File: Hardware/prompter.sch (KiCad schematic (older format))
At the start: 76 parts, among them J1 USB_B_Micro, J2 SWD, J3 L1, J4 L3, J5 PWR, J6 L2, J7 L4, J8 UART, Q1 AO3401A, SW1 PGM/RUN, SW2 SW_SPDT, SW3 SW_SPDT, SW4 SW_SPDT, SW5 SW_SPDT, U2 USBLC6-2P6, U3 STM32F405RGT6, U6 MP2359, Y1 16MHz

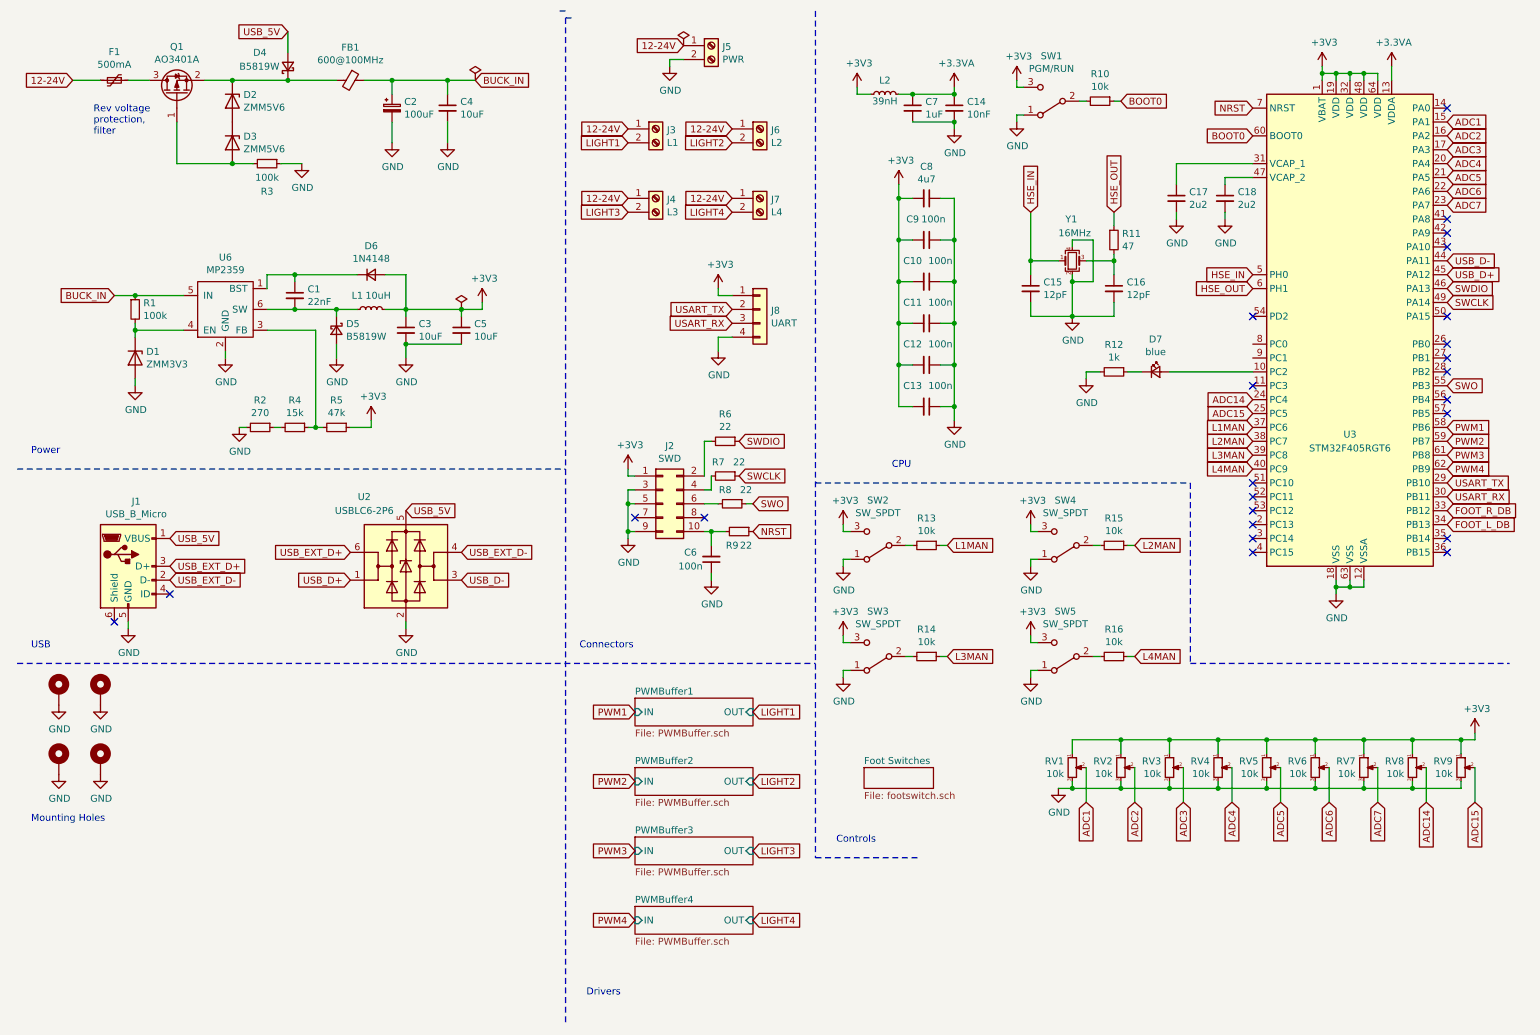
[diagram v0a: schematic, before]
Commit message: for future extension, also added DMX hardware
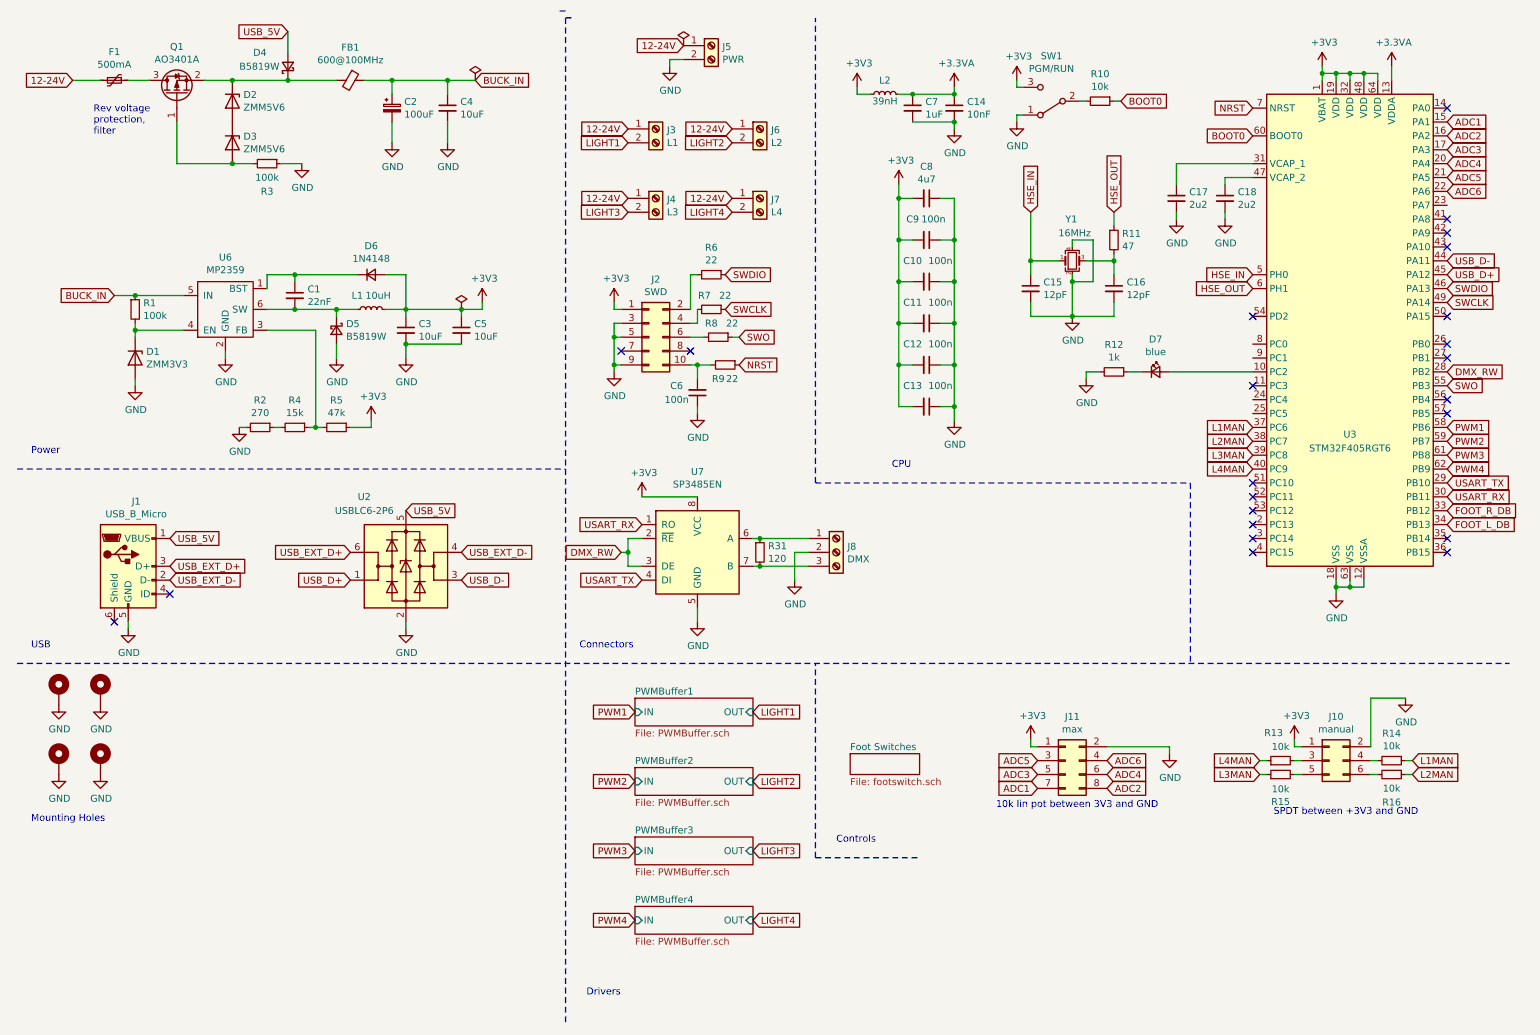
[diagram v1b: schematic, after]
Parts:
- removed J8: UART, Pin_Headers:Pin_Header_Straight_1x04_Pitch2.54mm, symbol Connector_Generic:Conn_01x04
- removed RV1, RV2, RV3, RV4, RV5, RV6, RV7, RV8, RV9: 10k, Pin_Headers:Pin_Header_Straight_1x03_Pitch2.54mm, symbol Device:R_POT_Small
- removed SW2, SW3, SW4, SW5: SW_SPDT, Pin_Headers:Pin_Header_Straight_1x03_Pitch2.54mm, symbol Switch:SW_SPDT
- added J10: manual, Pin_Headers:Pin_Header_Straight_2x03_Pitch2.54mm, symbol Connector_Generic:Conn_02x03_Odd_Even
- added J11: max, Pin_Headers:Pin_Header_Straight_2x04_Pitch2.54mm, symbol Connector_Generic:Conn_02x04_Odd_Even
- added J8: DMX, Connectors_Phoenix:PhoenixContact_MCV-G_03x3.50mm_Vertical, symbol Connector:Screw_Terminal_01x03
- added R31: 120, Resistors_SMD:R_0402, symbol Device:R_Small
- added U7: SP3485EN, Housings_SOIC:SOIC-8_3.9x4.9mm_Pitch1.27mm, symbol Interface_UART:SP3485EN
- J1: footprint Connectors:USB_Micro-B -> Connector_USB:USB_Micro-B_Amphenol_10104110_Horizontal
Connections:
- net +3V3: now also J10.1 (Pin_1), J11.1 (Pin_1), U7.8 (VCC)
- net ADC1: now also J11.7 (Pin_7)
- net ADC2: now also J11.8 (Pin_8)
- net ADC3: now also J11.5 (Pin_5)
- net ADC4: now also J11.6 (Pin_6)
- net ADC5: now also J11.3 (Pin_3)
- net ADC6: now also J11.4 (Pin_4)
- net GND: now also J10.2 (Pin_2), J11.2 (Pin_2), J8.2 (Pin_2), U7.5 (GND)
- net L1MAN: now also R14.1; no longer R13.1
- net L2MAN: now also R16.1; no longer R15.1
- net L3MAN: now also R15.1; no longer R14.1
- net L4MAN: now also R13.1; no longer R16.1
- net USART_RX: now also U7.1 (RO)
- net USART_TX: now also U7.4 (DI)
- net DMX_RW: now reaches U3.28 (PB2)
- net DMX_RW: now also U7.2 (~RE~), U7.3 (DE)
- net at R13.2: now also J10.3 (Pin_3)
- net at R15.2: now also J10.5 (Pin_5)
- net at R14.2: now also J10.4 (Pin_4)
- net at R16.2: now also J10.6 (Pin_6)
- net ADC14: no longer names the net of U3.24 (PC4)
- net ADC15: no longer names the net of U3.25 (PC5)
- net ADC7: no longer names the net of U3.23 (PA7)
- new net: J8.1 (Pin_1), R31.1, U7.6 (A)
- new net: J8.3 (Pin_3), R31.2, U7.7 (B)
- no-connect marks 24 -> 23
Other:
- note added: "10k lin pot between 3V3 and GND"
- note added: "SPDT between +3V3 and GND"
- moved on the sheet: C6, J2, R13, R14, R15, R16, R6, R7, R8, R9

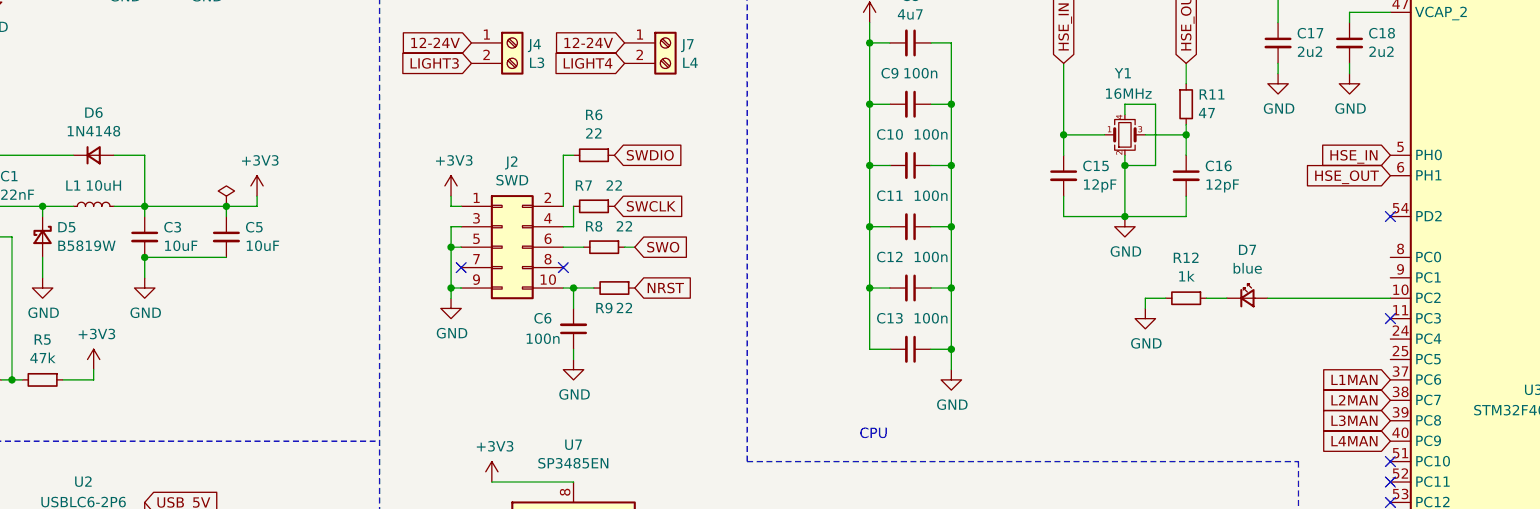
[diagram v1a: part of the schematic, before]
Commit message: Board updates:
Fixed footprints (SMD vs. THT, no hanging pads in the air)
Added mounting holes for production
Moved F.Fab text to readable locations
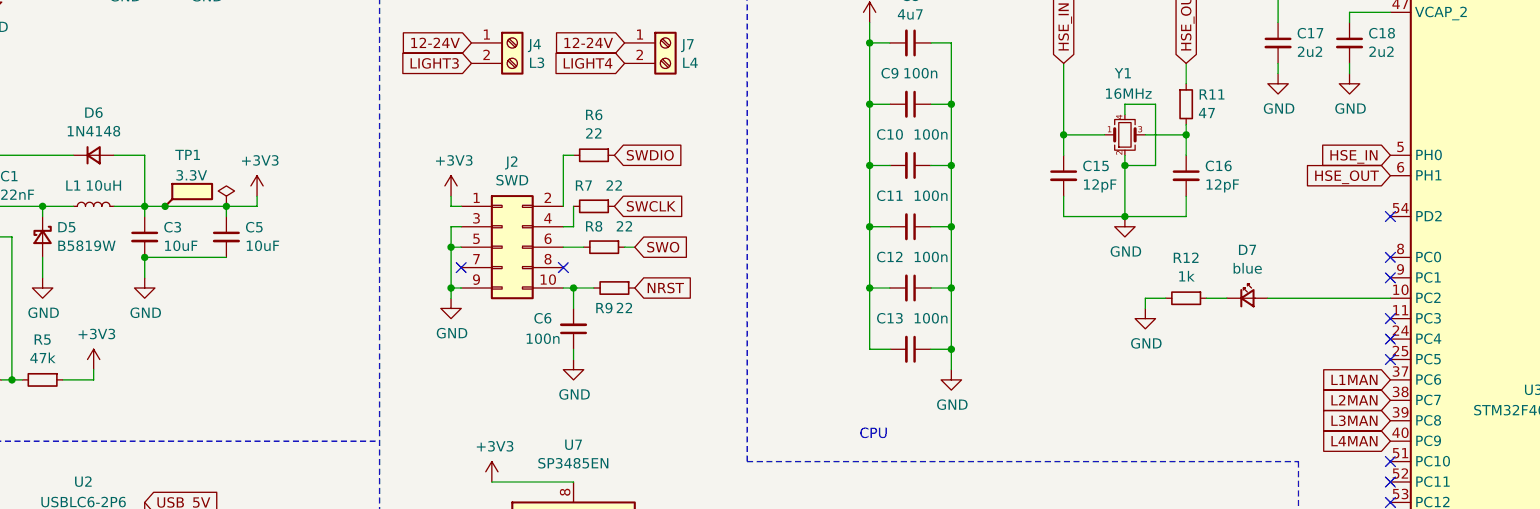
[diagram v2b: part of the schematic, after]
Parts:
- added TP1: 3.3V, Measurement_Points:Measurement_Point_Round-SMD-Pad_Small, symbol Connector:TestPoint_Flag
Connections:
- net +3V3: now also TP1.1
- no-connect marks 23 -> 27
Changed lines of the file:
@@
 $EndComp
 Wire Wire Line
-	3300 2600 3700 2600
+	3300 2600 3400 2600
 Connection ~ 3300 2600
 Wire Wire Line
@@
 Wire Wire Line
 	5850 4450 6200 4450
+NoConn ~ 9400 2850
+NoConn ~ 9400 2950
+NoConn ~ 9400 3250
+NoConn ~ 9400 3350
+$Comp
+L Connector:TestPoint_Flag TP1
+U 1 1 5FA2479D
+P 3400 2600
+F 0 "TP1" H 3450 2850 50  0000 L CNN
+F 1 "3.3V" H 3450 2750 50  0000 L CNN
+F 2 "Measurement_Points:Measurement_Point_Round-SMD-Pad_Small" H 3600 2600 50  0001 C CNN
+F 3 "~" H 3600 2600 50  0001 C CNN
+	1    3400 2600
+	1    0    0    -1
+$EndComp
+Connection ~ 3400 2600
+Wire Wire Line
+	3400 2600 3700 2600
 $EndSCHEMATC

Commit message: Hardware v0.1, Firmware runs ADC trigger by TIM3
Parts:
- C3, C4, C5: LCSC C15850 -> C13585
- J1: footprint Connector_USB:USB_Micro-B_Amphenol_10104110_Horizontal -> Hardware:USB_Micro-B
- L2: LCSC C26443 -> C86063
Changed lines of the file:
@@
 F 2 "Capacitors_SMD:C_1206" H 3600 1150 50  0001 C CNN
 F 3 "~" H 3600 1150 50  0001 C CNN
-F 4 "C15850" H 3600 1150 50  0001 C CNN "LCSC"
+F 4 "C13585" H 3600 1150 50  0001 C CNN "LCSC"
 	1    3600 1150
 	1    0    0    -1
@@
 F 2 "Capacitors_SMD:C_1206" H 3700 2750 50  0001 C CNN
 F 3 "~" H 3700 2750 50  0001 C CNN
-F 4 "C15850" H 3700 2750 50  0001 C CNN "LCSC"
+F 4 "C13585" H 3700 2750 50  0001 C CNN "LCSC"
 	1    3700 2750
 	1    0    0    -1
@@
 F 2 "Capacitors_SMD:C_1206" H 3300 2750 50  0001 C CNN
 F 3 "~" H 3300 2750 50  0001 C CNN
-F 4 "C15850" H 3300 2750 50  0001 C CNN "LCSC"
+F 4 "C13585" H 3300 2750 50  0001 C CNN "LCSC"
 	1    3300 2750
 	1    0    0    -1
@@
 F 2 "Resistors_SMD:R_0402" H 6750 1050 50  0001 C CNN
 F 3 "~" H 6750 1050 50  0001 C CNN
-F 4 "C26443" V 6750 1050 50  0001 C CNN "LCSC"
+F 4 "C86063" V 6750 1050 50  0001 C CNN "LCSC"
 	1    6750 1050
 	0    -1   -1   0
@@
 F 0 "J1" H 1357 4917 50  0000 C CNN
 F 1 "USB_B_Micro" H 1357 4826 50  0000 C CNN
-F 2 "Connector_USB:USB_Micro-B_Amphenol_10104110_Horizontal" H 1450 4400 50  0001 C CNN
+F 2 "Hardware:USB_Micro-B" H 1450 4400 50  0001 C CNN
 F 3 "~" H 1450 4400 50  0001 C CNN
 	1    1300 4450
